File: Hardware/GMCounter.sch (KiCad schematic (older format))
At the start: 58 parts, among them P1 GM_CONN, P10 TP, P11 TP, P12 TP, P13 TP, P14 TP, P2 TP, P3 TP, P4 TP, P5 BATT_CONN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

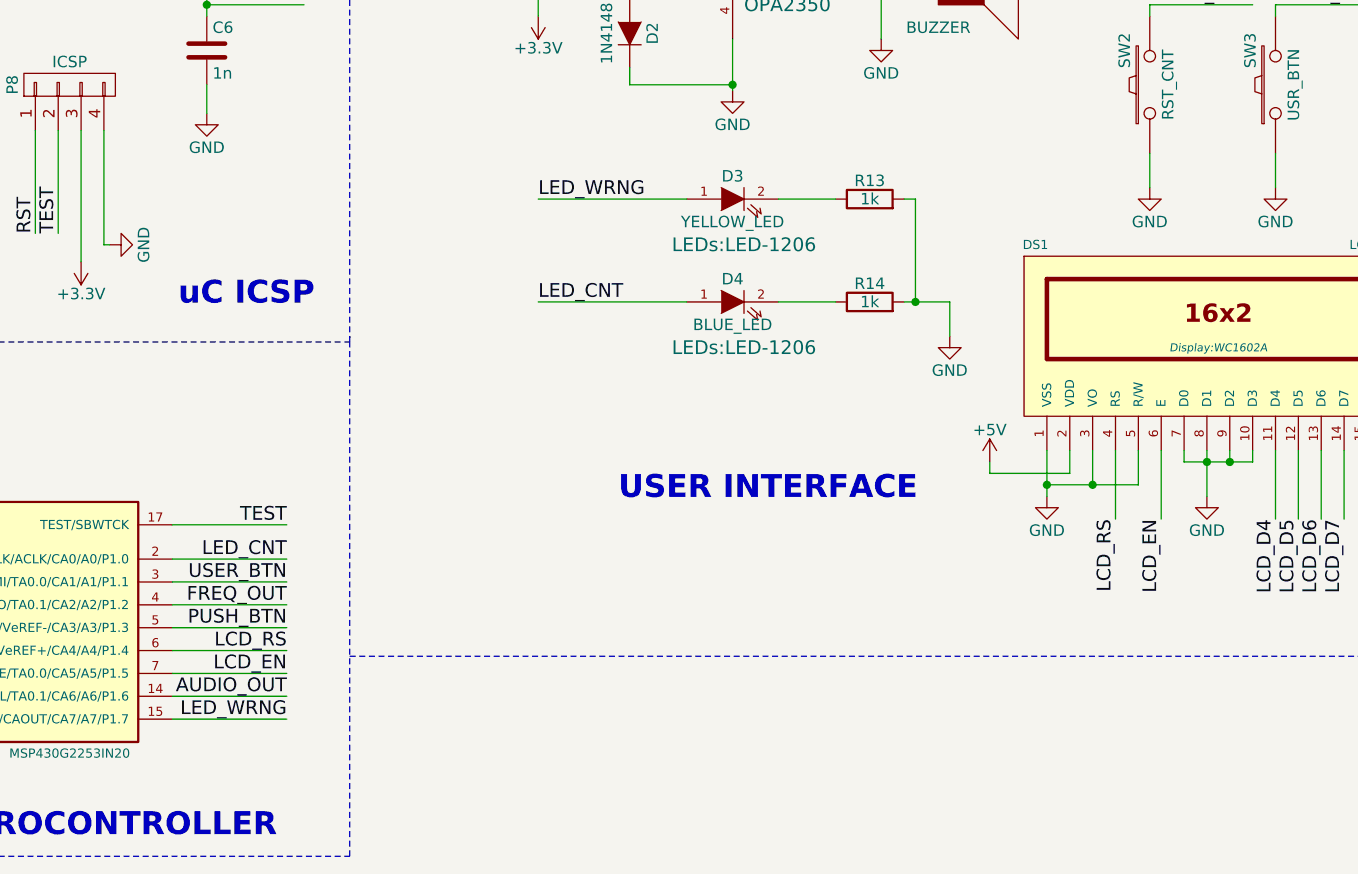
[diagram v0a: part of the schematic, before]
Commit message: Schematic design now includes potentiometer
Netlist has been exported, but it hasn't been imported to PCB yet
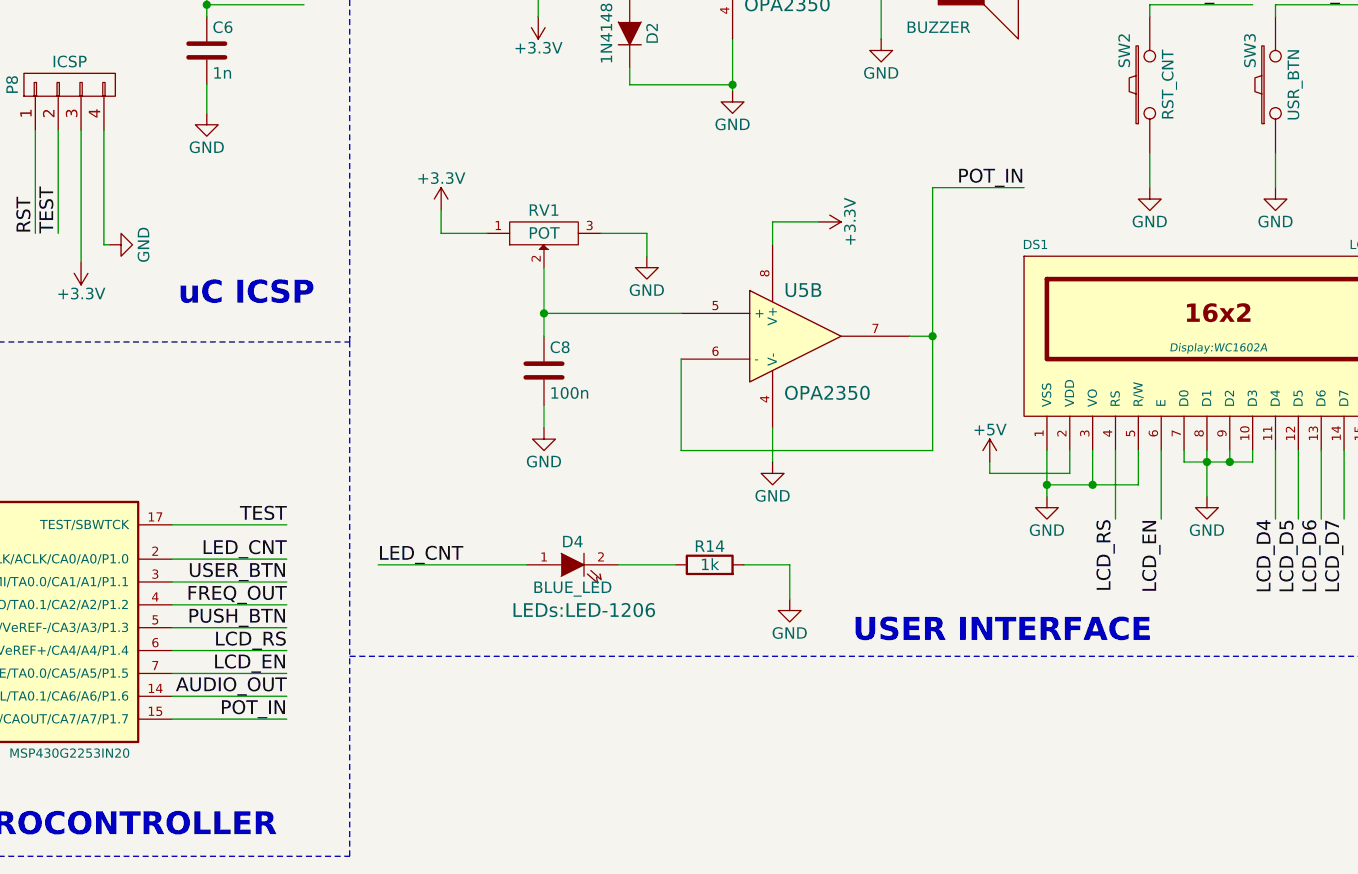
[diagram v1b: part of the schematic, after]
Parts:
- removed D3: YELLOW_LED, LEDs:LED-1206, symbol LED-RESCUE-GMCounter
- removed R13: 1k, Resistors_SMD:R_0805_HandSoldering, symbol R
- added C8: 100n, symbol C
- added RV1: POT, symbol POT
- added unit 2 of U5
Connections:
- net +3V3: now also RV1.1, U5.8 (V+)
- net GND: now also C8.2, RV1.3, U5.4 (V-)
- net LED_WRNG renamed POT_IN
- net POT_IN: now also U5.6 (-), U5.7
- new net: C8.1, RV1.2, U5.5 (+)
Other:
- moved on the sheet: D4, R14

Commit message: PCB Release Candidate
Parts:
- C8: footprint (none) -> Capacitors_SMD:C_0805_HandSoldering
- P14: footprint Measurement_Points:Measurement_Point_Round-TH_Small -> Pin_Headers:Pin_Header_Straight_1x01
- RV1: footprint (none) -> Potentiometers:Potentiometer_Alps-RK16-single_largePads
- U5: footprint (none) -> Housings_SOIC:SOIC-8_3.9x4.9mm_Pitch1.27mm
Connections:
- net +3V3: no longer U5.8 (V+)
- net +5V: now also U5.8 (V+)
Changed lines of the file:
@@
 F 0 "P14" H 10850 1150 50  0000 C CNN
 F 1 "TP" V 10950 1050 50  0000 C CNN
-F 2 "Measurement_Points:Measurement_Point_Round-TH_Small" H 10850 1050 60  0001 C CNN
+F 2 "Pin_Headers:Pin_Header_Straight_1x01" H 10850 1050 60  0001 C CNN
 F 3 "" H 10850 1050 60  0000 C CNN
 	1    10850 1050
@@
 F 0 "RV1" H 7150 4500 50  0000 C CNN
 F 1 "POT" H 7150 4600 50  0000 C CNN
-F 2 "" H 7150 4600 60  0000 C CNN
+F 2 "Potentiometers:Potentiometer_Alps-RK16-single_largePads" H 7150 4600 60  0001 C CNN
 F 3 "" H 7150 4600 60  0000 C CNN
 	1    7150 4600
@@
 F 0 "U5" H 8200 5250 60  0000 L CNN
 F 1 "OPA2350" H 8200 4800 60  0000 L CNN
-F 2 "" H 8250 5050 60  0000 C CNN
+F 2 "Housings_SOIC:SOIC-8_3.9x4.9mm_Pitch1.27mm" H 8250 5050 60  0001 C CNN
 F 3 "" H 8250 5050 60  0000 C CNN
 	2    8250 5050
 	1    0    0    -1
-$EndComp
-$Comp
-L +3.3V #PWR054
-U 1 1 56A28726
-P 8350 4550
-F 0 "#PWR054" H 8350 4400 50  0001 C CNN
-F 1 "+3.3V" H 8350 4690 50  0000 C CNN
-F 2 "" H 8350 4550 60  0000 C CNN
-F 3 "" H 8350 4550 60  0000 C CNN
-	1    8350 4550
-	0    1    1    0
 $EndComp
 $Comp
@@
 F 0 "C8" H 7175 5300 50  0000 L CNN
 F 1 "100n" H 7175 5100 50  0000 L CNN
-F 2 "" H 7188 5050 30  0000 C CNN
+F 2 "Capacitors_SMD:C_0805_HandSoldering" H 7188 5050 30  0001 C CNN
 F 3 "" H 7150 5200 60  0000 C CNN
 	1    7150 5200
@@
 $EndComp
 $Comp
-L GND #PWR055
+L GND #PWR054
 U 1 1 56A2E5CA
 P 8150 5600
-F 0 "#PWR055" H 8150 5350 50  0001 C CNN
+F 0 "#PWR054" H 8150 5350 50  0001 C CNN
 F 1 "GND" H 8150 5450 50  0000 C CNN
 F 2 "" H 8150 5600 60  0000 C CNN
@@
 $EndComp
 $Comp
-L GND #PWR056
+L GND #PWR055
 U 1 1 56A30724
 P 7150 5450
-F 0 "#PWR056" H 7150 5200 50  0001 C CNN
+F 0 "#PWR055" H 7150 5200 50  0001 C CNN
 F 1 "GND" H 7150 5300 50  0000 C CNN
 F 2 "" H 7150 5450 60  0000 C CNN
@@
 	8850 5050 8750 5050
 Wire Wire Line
-	8350 4550 8150 4550
-Wire Wire Line
-	8150 4550 8150 4650
-Wire Wire Line
 	8150 5600 8150 5450
 Wire Wire Line
@@
 Text Label 9250 4400 2    60   ~ 0
 POT_IN
+$Comp
+L +5V #PWR056
+U 1 1 56A2ABC5
+P 8150 4500
+F 0 "#PWR056" H 8150 4350 50  0001 C CNN
+F 1 "+5V" H 8150 4640 50  0000 C CNN
+F 2 "" H 8150 4500 60  0000 C CNN
+F 3 "" H 8150 4500 60  0000 C CNN
+	1    8150 4500
+	1    0    0    -1
+$EndComp
+Wire Wire Line
+	8150 4500 8150 4650
 $EndSCHEMATC

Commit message: PCB Release Candidate
v 0.3
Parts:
- removed U4: TPS76533, Housings_SOIC:SOIC-8_3.9x4.9mm_Pitch1.27mm, symbol TPS76533
- added P15: TP, Pin_Headers:Pin_Header_Straight_1x01, symbol CONN_01X01
- added U4: LD1117S33CTR, SOT-223, symbol LD1117S33CTR
- C3: footprint Capacitors_Elko_ThroughHole:Elko_vert_11.2x6.3mm_RM2.5 -> Capacitors_ThroughHole:C_Radial_D10_L20_P2.5-5
- C4: value 4u7 -> 22u; footprint Capacitors_Elko_ThroughHole:Elko_vert_11.2x6.3mm_RM2.5 -> Capacitors_ThroughHole:C_Radial_D10_L20_P2.5-5
- U3: footprint Housings_DIP:DIP-20_W7.62mm_LongPads -> Housings_SSOP:TSSOP-20_4.4x6.5mm_Pitch0.65mm
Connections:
- net +3V3: now also U4.2 (VO)
- net +5V: now also U4.3 (VI)
- net GND: now also P15.1 (P1), U4.1 (GND)
- no-connect marks 3 -> 1
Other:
- moved on the sheet: P7

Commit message: PCB Submission to SeeedStudio
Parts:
- added P16: TP, Measurement_Points:Measurement_Point_Round-TH_Small, symbol CONN_01X01
- DS1: footprint Display:WC1602A -> Socket_Strips:Socket_Strip_Straight_1x16
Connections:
- net GND: now also P16.1 (P1)
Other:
- moved on the sheet: P15
